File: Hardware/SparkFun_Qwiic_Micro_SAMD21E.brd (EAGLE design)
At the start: 25.4 x 25.4 mm, 75 parts, among them Q1 2.5A/30V/105mΩ, U1 3.3V, U2 W25Q32FV

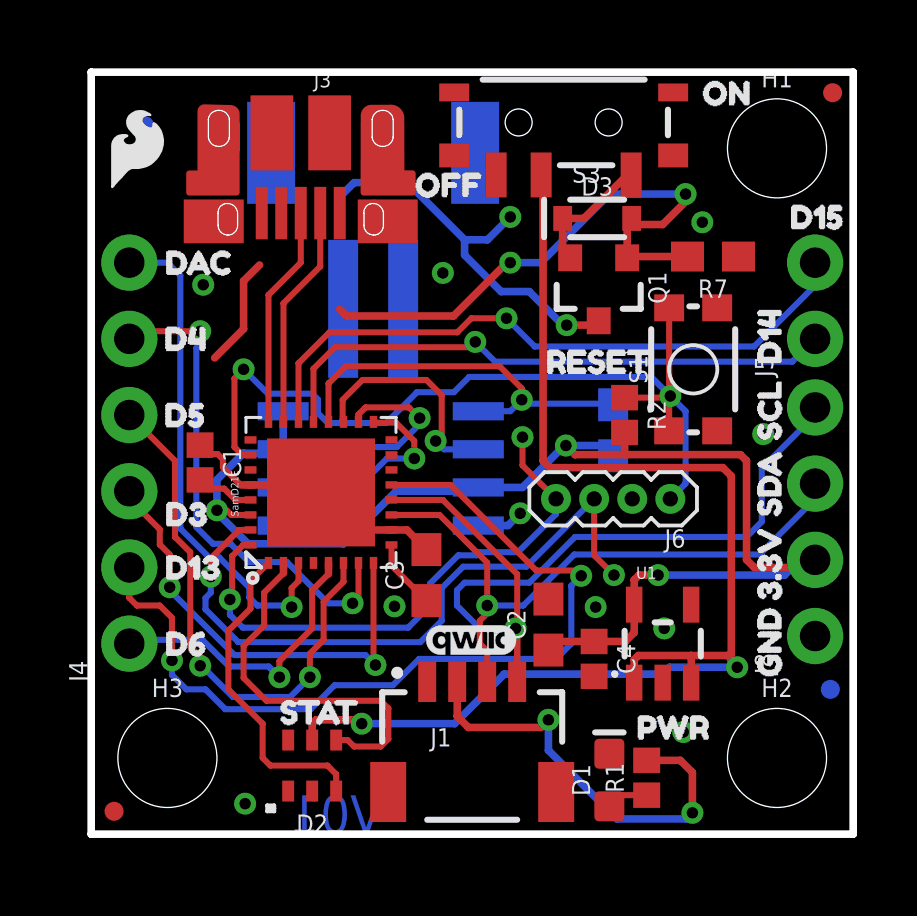
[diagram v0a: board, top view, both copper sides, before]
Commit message: Improves all silk, replaces 0603 resistor with 0402, updates trace work for better ground pour
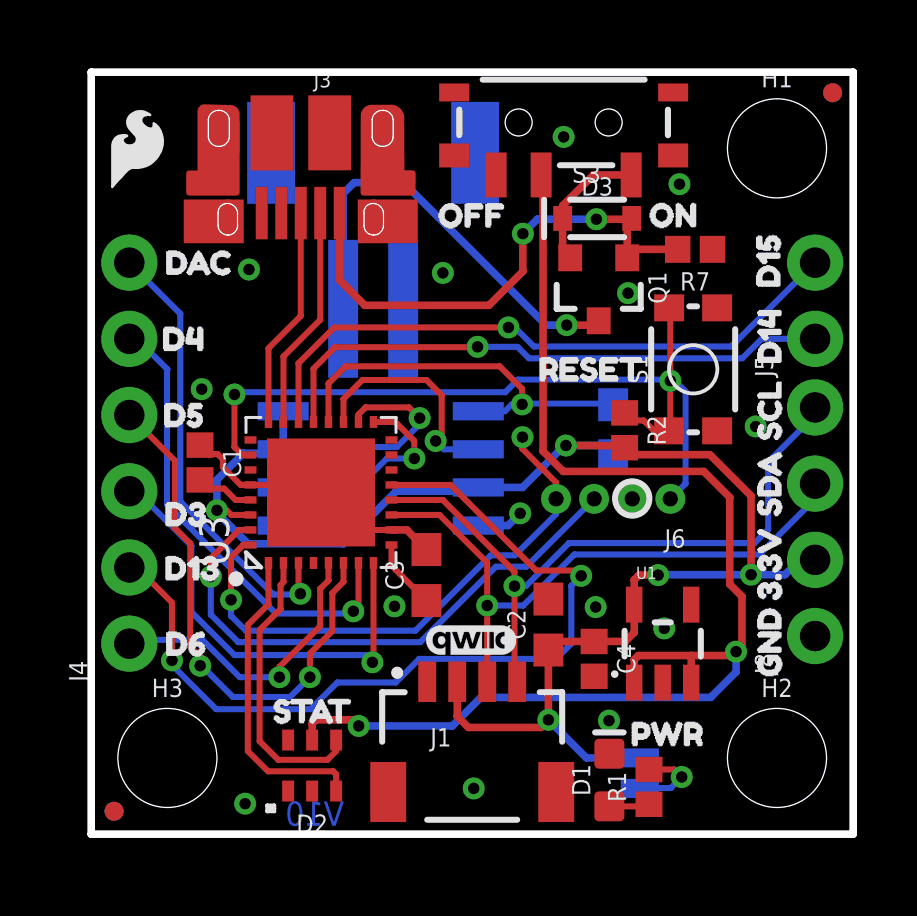
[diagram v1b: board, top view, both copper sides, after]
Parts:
- removed SAMD21E18: SAMD32E, Test:QFN32
- removed TP2, TP4: TEST-POINTTP_15TH_THRU, SparkFun-Connectors:TP_15TH
- added JP1: LED, SparkFun-Jumpers:SMT-JUMPER_2_NC_TRACE_SILK
- added U$23: (no value), SparkFun-Aesthetics:QWIIC_6MM
- added U$24: (no value), MICRO:LED1
- added U3: SAMD21E, Test:QFN32
- J6: device SparkFun-Connectors:1X04_1.27MM -> SparkFun-Connectors:1X04_1.27MM_NO_SILK
- Q1: value 2.5A/30V/105mΩ -> 3.1A/30V/105mΩ
- R7: device SparkFun-Resistors:0603 -> SparkFun-Resistors:0402
- U$11: device BUZZARD_BOTTOM:MOSI10 -> Underside Labels:D69
- U$12: device BUZZARD_BOTTOM:SCK12 -> Underside Labels:D138
- U$13: device BUZZARD_BOTTOM:D14#TX9 -> Underside Labels:DAC4
- U$14: device BUZZARD_BOTTOM:D15#RX10 -> MISO:MISO0
- U$15: device buzzard_labels:QWIIC_MICRO16 -> MICRO:MICRO0
- U$16: device BUZZARD_BOTTOM:D68 -> Underside Labels:MOSI5
- U$20: device BUZZARD_BOTTOM:D1313 -> Underside Labels:SCK7
- U$6: device BUZZARD_BOTTOM:D0#SDA2 -> Underside Labels:D0#SDA3
- U$7: device BUZZARD_BOTTOM:DAC9 -> Underside Labels:D2#SCL2
- U$8: device BUZZARD_BOTTOM:D2#SCL3 -> Underside Labels:D14#TX1
- U$9: device BUZZARD_BOTTOM:MISO11 -> Underside Labels:D15#RX0
- moved FD2 24.2 mm to (0.76, 0.76)
- moved FD3 23.0 mm to (24.7, 24.7)
- moved U$7 19.0 mm to (23.7, 14.2)
- moved U$9 19.0 mm to (23.7, 19.0)
- moved U$14 18.5 mm to (5.70, 14.0)
- moved U$13 18.5 mm to (5.22, 19.0)
- moved U$11 10.3 mm to (4.41, 6.29)
- moved U$16 10.1 mm to (5.82, 16.4)
- moved U$15 6.94 mm to (11.7, 5.08)
- moved U$46 4.44 mm to (17.9, 20.6)
- moved LOGO2 3.84 mm to (13.2, 7.62)
- moved U$22 3.42 mm to (14.2, 3.30)
- moved TP1 3.09 mm to (16.8, 20.5)
- moved U$42 3.05 mm to (22.6, 17.5), turned to 90 degrees
- moved U$12 2.65 mm to (4.85, 8.83)
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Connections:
- removed net N$1 (its old number): S3.1
- removed net VBATT: Q1.3, TP2.P$1
- removed net VUSB: D3.A, Q1.1, R7.2, TP1.P$1
- new net N$2: JP1.1, R1.2
- net !RESET: now also U3.RES; no longer SAMD21E18.NRESET
- net 3.3V: now also JP1.2, U3.VDDIN; no longer R1.2, SAMD21E18.VDDIN
- net CI: now also U3.PA01; no longer SAMD21E18.PA01
- net D+: now also U3.PA25; no longer SAMD21E18.PA25
- net D-: now also U3.PA24; no longer SAMD21E18.PA24
- net D13: now also U3.PA10; no longer SAMD21E18.PA10
- net D6: now also U3.PA04; no longer SAMD21E18.PA04
- net DAC: now also U3.PA02; no longer SAMD21E18.PA02
- net DI: now also U3.PA00; no longer SAMD21E18.PA00
- net FLASH_CS: now also U3.PA19; no longer SAMD21E18.PA19
- net FLASH_MISO: now also U3.PA18; no longer SAMD21E18.PA18
- net FLASH_MOSI: now also U3.PA16; no longer SAMD21E18.PA16
- net FLASH_SCK: now also U3.PA17; no longer SAMD21E18.PA17
- net GND: now also U3.GND, U3.GNDANA, U3.PAD; no longer SAMD21E18.GND, SAMD21E18.GNDANA, SAMD21E18.PAD
- net MISO: now also U3.PA05; no longer SAMD21E18.PA05
- net MOSI: now also U3.PA06; no longer SAMD21E18.PA06
- net RX: now also U3.PA23; no longer SAMD21E18.PA23
- net SCK: now also U3.PA07; no longer SAMD21E18.PA07
- net SCL: now also U3.PA09; no longer SAMD21E18.PA09
- net SDA: now also U3.PA08; no longer SAMD21E18.PA08
- net SWCLK: now also U3.PA30; no longer SAMD21E18.PA30, TP4.P$1
- net SWDIO: now also U3.PA31; no longer SAMD21E18.PA31
- net TX: now also U3.PA22; no longer SAMD21E18.PA22
- net VDDA: now also U3.VDD; no longer SAMD21E18.VDDANA
- net VDDCORE: now also U3.VDDCORE; no longer SAMD21E18.VDDCORE
- net V_BATT: now also Q1.3
- net V_USB: now also D3.A, Q1.1, R7.2, TP1.P$1
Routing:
- net VUSB: track 19.2 -> 0.00 mm, vias 1 -> 0
- net V_USB: track 0.00 -> 17.4 mm, vias 0 -> 1
- net V_BATT: track 0.00 -> 14.5 mm, vias 0 -> 1
- net VBATT: track 12.8 -> 0.00 mm, vias 1 -> 0
- net 3.3V: track 60.4 -> 52.3 mm
- net SCL: track 29.6 -> 22.8 mm
- net GND: track 14.4 -> 10.7 mm, vias 10 -> 14
- net SWCLK: track 22.3 -> 18.7 mm
- net CI: track 12.6 -> 9.57 mm
- net N$2: track 0.00 -> 2.75 mm, vias 0 -> 1
- net DAC: track 16.9 -> 15.0 mm
- net !RESET: track 29.0 -> 27.5 mm
- net MOSI: track 16.7 -> 15.6 mm, vias 2 -> 1
- net RX: track 21.8 -> 21.1 mm
- net SCK: track 15.2 -> 15.1 mm, vias 2 -> 1
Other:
- board text added: "V10"
- board text removed: "V01"

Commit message: Moves some traces
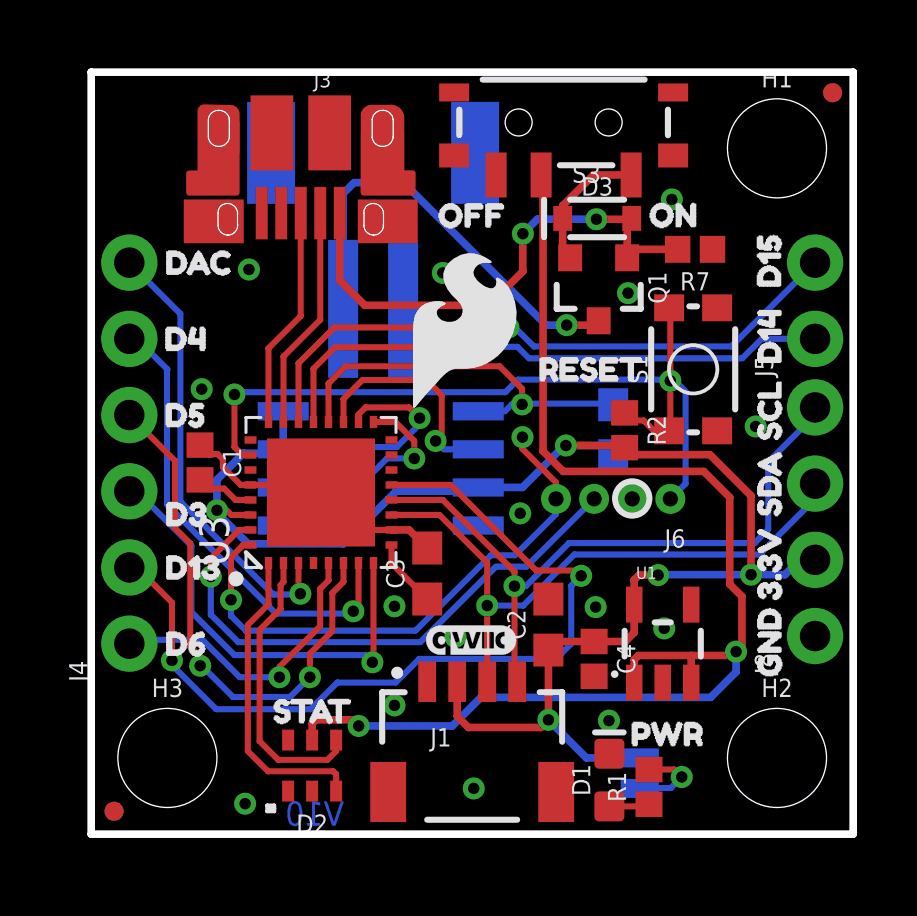
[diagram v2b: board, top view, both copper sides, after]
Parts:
- LOGO3: value SFE_LOGO_FLAME.1_INCH -> SFE_LOGO_FLAME.2_INCH; device SparkFun-Aesthetics:SFE_LOGO_FLAME_.1 -> SparkFun-Aesthetics:SFE_LOGO_FLAME_.2
- U$18: device BUZZARD_BOTTOM:OFF12 -> buzzard_labels:ON12
- U$19: device BUZZARD_BOTTOM:ON11 -> buzzard_labels:OFF13
- moved LOGO3 12.5 mm to (12.4, 16.8)
- moved U$18 5.99 mm to (20.9, 20.6), turned to 0 degrees
- moved U$19 1.36 mm to (17.1, 20.6), turned to 0 degrees
- moved LOGO1 0.57 mm to (1.52, 23.1)
- moved U$15 0.09 mm to (11.6, 5.13)
- moved U$37 0.08 mm to (1.78, 16.5)
- moved C3 0.06 mm to (11.2, 8.69)
- moved U$38 0.05 mm to (1.79, 14.0)
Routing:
- net GND: track 10.7 -> 9.15 mm, vias 14 -> 15

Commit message: Updates micro-controller symbol with Arduino digital pin assignments
* replaces lipo battery symbol with better one
* Re-adds battery line test ponit
* Removes info text about Arduino pin assignments
* Improves notes on SERCOM ports
* Re-numbers all parts
* Removes test library - no longer needed.
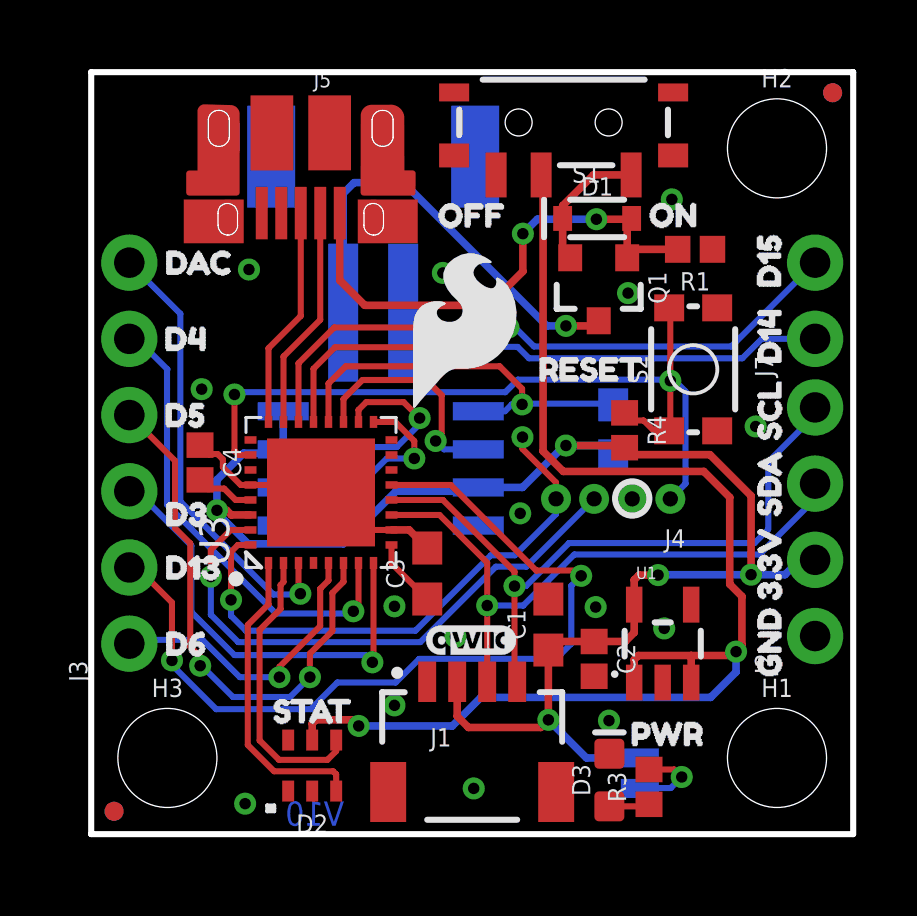
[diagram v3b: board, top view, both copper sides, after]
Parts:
- removed J8: (no value), SparkFun-Connectors:1X04_NO_SILK
- removed R7: 10k, SparkFun-Resistors:0402
- removed S3: (no value), SparkFun-Switches:SWITCH_SPST_SMD_A
- added J7: (no value), SparkFun-Connectors:1X02_NO_SILK
- added R4: 10k, SparkFun-Resistors:0402
- added S2: MOMENTARY-SWITCH-SPST-SMD-4.6X2.8MM, SparkFun-Switches:TACTILE_SWITCH_SMD_4.6X2.8MM
- added TP2: TEST-POINTTP_15TH_THRU, SparkFun-Connectors:TP_15TH
- C1: value 1.0uF -> 10uF; device SparkFun-Capacitors:0402 -> SparkFun-Capacitors:0603
- C2: value 10uF -> 1.0uF; device SparkFun-Capacitors:0603 -> SparkFun-Capacitors:0402
- D1: value RED -> 1A/23V/620mV; device SparkFun-LED:LED-0603 -> SparkFun-DiscreteSemi:SOD-323
- D3: value 1A/23V/620mV -> RED; device SparkFun-DiscreteSemi:SOD-323 -> SparkFun-LED:LED-0603
- J2: device SparkFun-Connectors:JST-2-SMD -> SparkFun-Connectors:1X04_NO_SILK
- J3: device SparkFun-Connectors:USB-MICROB-PTH-MILL -> SparkFun-Connectors:1X06_NO_SILK
- J4: device SparkFun-Connectors:1X06_NO_SILK -> SparkFun-Connectors:1X04_1.27MM_NO_SILK
- J5: device SparkFun-Connectors:1X02_NO_SILK -> SparkFun-Connectors:USB-MICROB-PTH-MILL
- J6: device SparkFun-Connectors:1X04_1.27MM_NO_SILK -> SparkFun-Connectors:JST-2-SMD
- LOGO1: value OSHW-LOGOS -> SFE_LOGO_NAME.1_INCH; device SparkFun-Aesthetics:OSHW-LOGO-S -> SparkFun-Aesthetics:SFE_LOGO_NAME_.1
- LOGO2: value SFE_LOGO_NAME.1_INCH -> SFE_LOGO_FLAME.2_INCH; device SparkFun-Aesthetics:SFE_LOGO_NAME_.1 -> SparkFun-Aesthetics:SFE_LOGO_FLAME_.2
- LOGO3: value SFE_LOGO_FLAME.2_INCH -> OSHW-LOGOS; device SparkFun-Aesthetics:SFE_LOGO_FLAME_.2 -> SparkFun-Aesthetics:OSHW-LOGO-S
- R1: value 1K -> 10k
- R2: device SparkFun-Resistors:0402 -> SparkFun-Resistors:0603
- R3: value 10k -> 1K; device SparkFun-Resistors:0603 -> SparkFun-Resistors:0402
- S1: value MOMENTARY-SWITCH-SPST-SMD-4.6X2.8MM -> (none); device SparkFun-Switches:TACTILE_SWITCH_SMD_4.6X2.8MM -> SparkFun-Switches:SWITCH_SPST_SMD_A
- U3: device Test:QFN32 -> SparkFun-IC-Microcontroller:QFN32
- moved FD1 33.9 mm to (24.7, 24.7), flipped to the bottom
- moved FD4 33.9 mm to (0.76, 0.76), flipped to the bottom
- moved J2 20.7 mm to (24.1, 6.60), flipped to the top, turned to 90 degrees
- moved H1 20.3 mm to (22.9, 2.54)
- moved H2 20.3 mm to (22.9, 22.9)
- moved LOGO1 19.4 mm to (13.2, 7.62)
- moved D1 18.7 mm to (16.9, 20.5), turned to 0 degrees
- moved D3 18.7 mm to (17.3, 1.80), turned to 90 degrees
- moved J4 18.7 mm to (19.3, 11.2), turned to 180 degrees
- moved R1 18.0 mm to (20.1, 19.5), turned to 180 degrees
- moved J5 17.6 mm to (6.99, 20.7), turned to 180 degrees
- moved J3 15.4 mm to (1.27, 6.35), turned to 90 degrees
- moved C4 14.7 mm to (3.63, 12.4)
- moved J6 14.0 mm to (9.40, 21.1), flipped to the bottom, turned to 0 degrees
- moved C1 12.8 mm to (15.2, 6.99), turned to 90 degrees
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- renumbered U$1 to LOGO4
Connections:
- net !RESET: now also J4.1, R4.1, S2.3, S2.4; no longer J6.1, R2.1, S1.3, S1.4
- net 3.3V: now also C1.1, J2.2, R4.2; no longer C4.1, J8.2, R3.2
- net D+: now also J5.D+; no longer J3.D+
- net D-: now also J5.D-; no longer J3.D-
- net D13: now also J3.2; no longer J4.2
- net D6: now also J3.1; no longer J4.1
- net DAC: now also J3.6; no longer J4.6
- net FLASH_CS: now also R2.1; no longer R3.1
- net GND: now also C1.2, C4.1, D3.C, J4.2, J5.GND, J5.SHIELD, J5.SHIELD10, J5.SHIELD2, J5.SHIELD3, J5.SHIELD4, J5.SHIELD5, J5.SHIELD6, J5.SHIELD7, J5.SHIELD8, J5.SHIELD9, J6.1, R1.1, S2.1, S2.2; no longer C1.1, C4.2, D1.C, J3.GND, J3.SHIELD, J3.SHIELD10, J3.SHIELD2, J3.SHIELD3, J3.SHIELD4, J3.SHIELD5, J3.SHIELD6, J3.SHIELD7, J3.SHIELD8, J3.SHIELD9, J6.2, J8.1, R7.1, S1.1, S1.2
- net MISO: now also J3.4; no longer J4.4
- net MOSI: now also J3.5; no longer J4.5
- net N$1: now also D3.A, R3.1; no longer D1.A, R1.1
- net N$2: now also R3.2; no longer R1.2
- net RX: now also J7.2; no longer J5.2
- net SCK: now also J3.3; no longer J4.3
- net SCL: now also J2.4; no longer J8.4
- net SDA: now also J2.3; no longer J8.3
- net SWCLK: now also J4.3; no longer J6.3
- net SWDIO: now also J4.4; no longer J6.4
- net TX: now also J7.1; no longer J5.1
- net VDDCORE: now also C4.2; no longer C1.2
- net VIN: now also S1.2; no longer S3.2
- net VIN1: now also D1.C, S1.3; no longer D3.C, S3.3
- net V_BATT: now also J6.2, TP2.P$1; no longer J2.2
- net V_USB: now also D1.A, J5.VBUS, R1.2; no longer D3.A, J3.VBUS, R7.2
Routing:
- net V_BATT: track 14.5 -> 14.7 mm, vias 1 -> 0
